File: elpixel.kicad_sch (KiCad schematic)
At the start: 6 parts, among them J1 Conn_01x02, J2 Conn_01x03, J3 Conn_01x03, Q1 BC857, U1 MC78M05_TO252, U2 WS2811

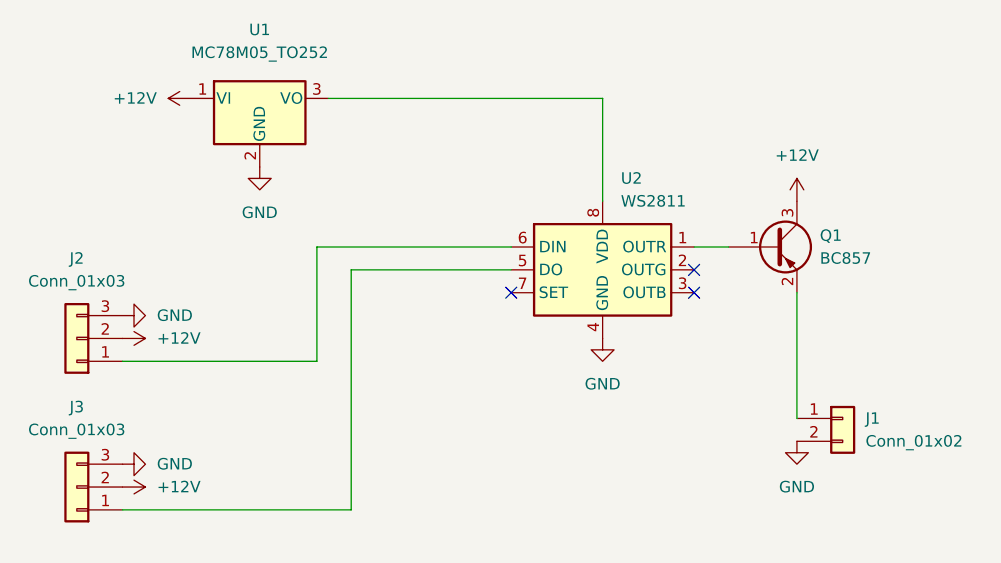
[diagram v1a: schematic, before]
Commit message: updated schematic for 6v passthrough
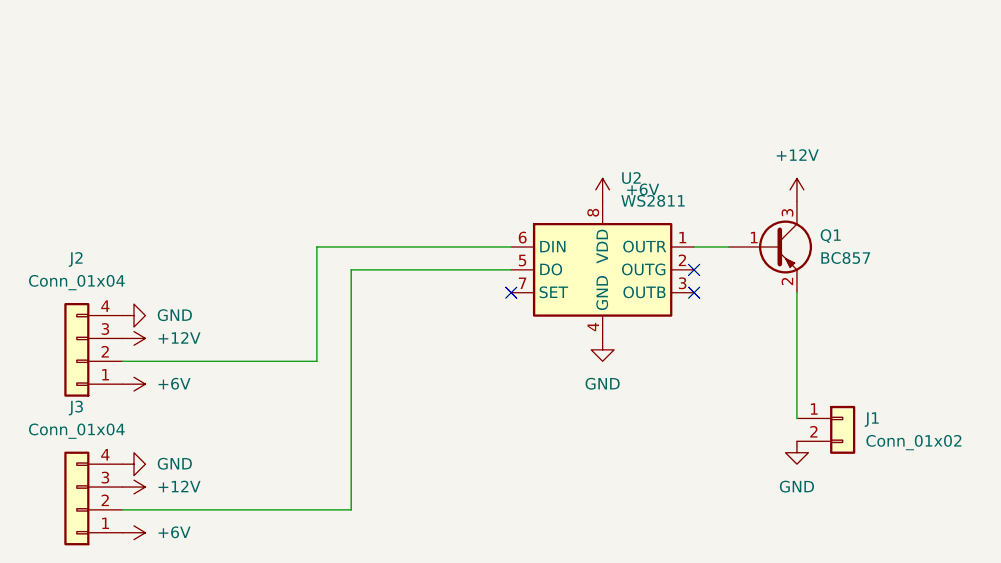
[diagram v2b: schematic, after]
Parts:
- removed J2, J3: Conn_01x03, Connector_PinHeader_1.00mm:PinHeader_1x03_P1.00mm_Vertical, symbol Connector_Generic:Conn_01x03
- removed U1: MC78M05_TO252, Package_TO_SOT_SMD:TO-252-2, symbol Regulator_Linear:MC78M05_TO252
- added J2, J3: Conn_01x04, Connector_PinHeader_2.54mm:PinHeader_1x04_P2.54mm_Vertical, symbol Connector_Generic:Conn_01x04
- J1: footprint Connector_PinHeader_1.00mm:PinHeader_1x02_P1.00mm_Vertical -> Connector_PinHeader_2.54mm:PinHeader_1x02_P2.54mm_Vertical
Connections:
- net +12V: now also J2.3 (Pin_3), J3.3 (Pin_3)
- net GND: now also J2.4 (Pin_4), J3.4 (Pin_4)
- net +6V: now reaches U2.8 (VDD)
- net +6V: now also J2.1 (Pin_1), J3.1 (Pin_1)
- net at U2.6 (DIN): now also J2.2 (Pin_2)
- net at U2.5 (DO): now also J3.2 (Pin_2)
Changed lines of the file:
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@@
-    (stroke (width 0) (type default) (color 0 0 0 0))
-  )
-  (wire (pts (xy 144.78 86.36) (xy 114.3 86.36))
     (stroke (width 0) (type default) (color 0 0 0 0))
   )
@@
     (stroke (width 0) (type default) (color 0 0 0 0))
   )
-  (wire (pts (xy 144.78 97.79) (xy 144.78 86.36))
-    (stroke (width 0) (type default) (color 0 0 0 0))
-  )
   (wire (pts (xy 154.94 102.87) (xy 158.75 102.87))
     (stroke (width 0) (type default) (color 0 0 0 0))
@@
     (stroke (width 0) (type default) (color 0 0 0 0))
   )
-  (symbol (lib_id "power:GND") (at 106.68 93.98 0) (unit 1)
-    (in_bom yes) (on_board yes) (fields_autoplaced)
-    (property "Reference" "#PWR02" (id 0) (at 106.68 100.33 0)
-      (effects (font (size 1.27 1.27)) hide)
-    )
-    (property "Value" "GND" (id 1) (at 106.68 99.06 0))
-    (property "Footprint" "" (id 2) (at 106.68 93.98 0)
-      (effects (font (size 1.27 1.27)) hide)
-    )
-    (property "Datasheet" "" (id 3) (at 106.68 93.98 0)
-      (effects (font (size 1.27 1.27)) hide)
-    )
-    (pin "1")
-  )
-  (symbol (lib_id "Regulator_Linear:MC78M05_TO252") (at 106.68 86.36 0) (unit 1)
-    (in_bom yes) (on_board yes) (fields_autoplaced)
-    (property "Reference" "U1" (id 0) (at 106.68 78.74 0))
-    (property "Value" "MC78M05_TO252" (id 1) (at 106.68 81.28 0))
-    (property "Footprint" "Package_TO_SOT_SMD:TO-252-2" (id 2) (at 106.68 80.645 0)
-      (effects (font (size 1.27 1.27) italic) hide)
-    )
-    (property "Datasheet" "https://www.onsemi.com/pub/Collateral/MC78M00-D.PDF" (id 3) (at 106.68 87.63 0)
+  (symbol (lib_id "Connector_Generic:Conn_01x04") (at 86.36 132.08 180) (unit 1)
+    (in_bom yes) (on_board yes) (fields_autoplaced)
+    (property "Reference" "J3" (id 0) (at 86.36 120.65 0))
+    (property "Value" "Conn_01x04" (id 1) (at 86.36 123.19 0))
+    (property "Footprint" "Connector_PinHeader_2.54mm:PinHeader_1x04_P2.54mm_Vertical" (id 2) (at 86.36 132.08 0)
+      (effects (font (size 1.27 1.27)) hide)
+    )
+    (property "Datasheet" "~" (id 3) (at 86.36 132.08 0)
       (effects (font (size 1.27 1.27)) hide)
     )
@@
     (pin "2")
     (pin "3")
-  )
-  (symbol (lib_id "Connector_Generic:Conn_01x03") (at 86.36 113.03 180) (unit 1)
+    (pin "4")
+  )
+  (symbol (lib_id "Connector_Generic:Conn_01x04") (at 86.36 115.57 180) (unit 1)
     (in_bom yes) (on_board yes) (fields_autoplaced)
     (property "Reference" "J2" (id 0) (at 86.36 104.14 0))
-    (property "Value" "Conn_01x03" (id 1) (at 86.36 106.68 0))
-    (property "Footprint" "Connector_PinHeader_1.00mm:PinHeader_1x03_P1.00mm_Vertical" (id 2) (at 86.36 113.03 0)
-      (effects (font (size 1.27 1.27)) hide)
-    )
-    (property "Datasheet" "~" (id 3) (at 86.36 113.03 0)
+    (property "Value" "Conn_01x04" (id 1) (at 86.36 106.68 0))
+    (property "Footprint" "Connector_PinHeader_2.54mm:PinHeader_1x04_P2.54mm_Vertical" (id 2) (at 86.36 115.57 0)
+      (effects (font (size 1.27 1.27)) hide)
+    )
+    (property "Datasheet" "~" (id 3) (at 86.36 115.57 0)
       (effects (font (size 1.27 1.27)) hide)
     )
@@
     (pin "2")
     (pin "3")
-  )
-  (symbol (lib_id "power:+12V") (at 99.06 86.36 90) (unit 1)
-    (in_bom yes) (on_board yes) (fields_autoplaced)
-    (property "Reference" "#PWR01" (id 0) (at 102.87 86.36 0)
-      (effects (font (size 1.27 1.27)) hide)
-    )
-    (property "Value" "+12V" (id 1) (at 95.25 86.3599 90)
-      (effects (font (size 1.27 1.27)) (justify left))
-    )
-    (property "Footprint" "" (id 2) (at 99.06 86.36 0)
-      (effects (font (size 1.27 1.27)) hide)
-    )
-    (property "Datasheet" "" (id 3) (at 99.06 86.36 0)
+    (pin "4")
+  )
+  (symbol (lib_id "power:+6V") (at 91.44 134.62 270) (unit 1)
+    (in_bom yes) (on_board yes) (fields_autoplaced)
+    (property "Reference" "#PWR0106" (id 0) (at 87.63 134.62 0)
+      (effects (font (size 1.27 1.27)) hide)
+    )
+    (property "Value" "+6V" (id 1) (at 95.25 134.6199 90)
+      (effects (font (size 1.27 1.27)) (justify left))
+    )
+    (property "Footprint" "" (id 2) (at 91.44 134.62 0)
+      (effects (font (size 1.27 1.27)) hide)
+    )
+    (property "Datasheet" "" (id 3) (at 91.44 134.62 0)
       (effects (font (size 1.27 1.27)) hide)
     )
@@
     )
     (pin "1")
-  )
-  (symbol (lib_id "Connector_Generic:Conn_01x03") (at 86.36 129.54 180) (unit 1)
-    (in_bom yes) (on_board yes) (fields_autoplaced)
-    (property "Reference" "J3" (id 0) (at 86.36 120.65 0))
-    (property "Value" "Conn_01x03" (id 1) (at 86.36 123.19 0))
-    (property "Footprint" "Connector_PinHeader_1.00mm:PinHeader_1x03_P1.00mm_Vertical" (id 2) (at 86.36 129.54 0)
-      (effects (font (size 1.27 1.27)) hide)
-    )
-    (property "Datasheet" "~" (id 3) (at 86.36 129.54 0)
-      (effects (font (size 1.27 1.27)) hide)
-    )
-    (pin "1")
-    (pin "2")
-    (pin "3")
   )
   (symbol (lib_id "power:+12V") (at 91.44 113.03 270) (unit 1)
@@
     (pin "1")
   )
+  (symbol (lib_id "power:+6V") (at 144.78 97.79 0) (unit 1)
+    (in_bom yes) (on_board yes) (fields_autoplaced)
+    (property "Reference" "#PWR0107" (id 0) (at 144.78 101.6 0)
+      (effects (font (size 1.27 1.27)) hide)
+    )
+    (property "Value" "+6V" (id 1) (at 147.32 96.5199 0)
+      (effects (font (size 1.27 1.27)) (justify left))
+    )
+    (property "Footprint" "" (id 2) (at 144.78 97.79 0)
+      (effects (font (size 1.27 1.27)) hide)
+    )
+    (property "Datasheet" "" (id 3) (at 144.78 97.79 0)
+      (effects (font (size 1.27 1.27)) hide)
+    )
+    (pin "1")
+  )
   (symbol (lib_id "power:+12V") (at 91.44 129.54 270) (unit 1)
     (in_bom yes) (on_board yes) (fields_autoplaced)
@@
     (pin "1")
   )
+  (symbol (lib_id "power:+6V") (at 91.44 118.11 270) (unit 1)
+    (in_bom yes) (on_board yes) (fields_autoplaced)
+    (property "Reference" "#PWR0105" (id 0) (at 87.63 118.11 0)
+      (effects (font (size 1.27 1.27)) hide)
+    )
+    (property "Value" "+6V" (id 1) (at 95.25 118.1099 90)
+      (effects (font (size 1.27 1.27)) (justify left))
+    )
+    (property "Footprint" "" (id 2) (at 91.44 118.11 0)
+      (effects (font (size 1.27 1.27)) hide)
+    )
+    (property "Datasheet" "" (id 3) (at 91.44 118.11 0)
+      (effects (font (size 1.27 1.27)) hide)
+    )
+    (pin "1")
+  )
   (symbol (lib_id "Connector_Generic:Conn_01x02") (at 171.45 121.92 0) (unit 1)
     (in_bom yes) (on_board yes) (fields_autoplaced)
@@
       (effects (font (size 1.27 1.27)) (justify left))
     )
-    (property "Footprint" "Connector_PinHeader_1.00mm:PinHeader_1x02_P1.00mm_Vertical" (id 2) (at 171.45 121.92 0)
+    (property "Footprint" "Connector_PinHeader_2.54mm:PinHeader_1x02_P2.54mm_Vertical" (id 2) (at 171.45 121.92 0)
       (effects (font (size 1.27 1.27)) hide)
     )
@@
   )
   (symbol_instances
-    (path "/47d22e24-7c7f-4617-a22e-884660a7a8ff"
-      (reference "#PWR01") (unit 1) (value "+12V") (footprint "")
-    )
-    (path "/2efe1230-4a03-4e1d-9162-464c7098deda"
-      (reference "#PWR02") (unit 1) (value "GND") (footprint "")
-    )
     (path "/8f921adc-1747-4800-9ac3-01ad2a3fd633"
       (reference "#PWR03") (unit 1) (value "GND") (footprint "")
@@
       (reference "#PWR0104") (unit 1) (value "GND") (footprint "")
     )
+    (path "/e3d64774-9e78-40c1-9325-685f973ec399"
+      (reference "#PWR0105") (unit 1) (value "+6V") (footprint "")
+    )
+    (path "/4d87b157-ce70-4012-a0d9-87eb85e410f2"
+      (reference "#PWR0106") (unit 1) (value "+6V") (footprint "")
+    )
+    (path "/a2e9fa44-79c9-4067-846e-ae22d942b353"
+      (reference "#PWR0107") (unit 1) (value "+6V") (footprint "")
+    )
     (path "/f81cf28d-7f8a-45aa-8733-bbbd77ce5ecf"
-      (reference "J1") (unit 1) (value "Conn_01x02") (footprint "Connector_PinHeader_1.00mm:PinHeader_1x02_P1.00mm_Vertical")
-    )
-    (path "/35766383-03d6-4f8b-9c16-d16020f426e2"
-      (reference "J2") (unit 1) (value "Conn_01x03") (footprint "Connector_PinHeader_1.00mm:PinHeader_1x03_P1.00mm_Vertical")
-    )
-    (path "/53789ae3-c50a-44f5-975b-fe54d0b54fab"
-      (reference "J3") (unit 1) (value "Conn_01x03") (footprint "Connector_PinHeader_1.00mm:PinHeader_1x03_P1.00mm_Vertical")
+      (reference "J1") (unit 1) (value "Conn_01x02") (footprint "Connector_PinHeader_2.54mm:PinHeader_1x02_P2.54mm_Vertical")
+    )
+    (path "/47e3616e-9142-4816-b15e-ecb20539f953"
+      (reference "J2") (unit 1) (value "Conn_01x04") (footprint "Connector_PinHeader_2.54mm:PinHeader_1x04_P2.54mm_Vertical")
+    )
+    (path "/16110478-ee5f-4d15-abfb-9d55e40b817e"
+      (reference "J3") (unit 1) (value "Conn_01x04") (footprint "Connector_PinHeader_2.54mm:PinHeader_1x04_P2.54mm_Vertical")
     )
     (path "/d6dc534e-6e8d-415a-9caa-ec4f0dc84478"
       (reference "Q1") (unit 1) (value "BC857") (footprint "Package_TO_SOT_SMD:SOT-23")
     )
-    (path "/33064f56-88c0-44a1-ac52-96957fe5ad49"
-      (reference "U1") (unit 1) (value "MC78M05_TO252") (footprint "Package_TO_SOT_SMD:TO-252-2")
-    )
     (path "/7e0ec61e-0a2f-41c6-9535-347b5902df41"
